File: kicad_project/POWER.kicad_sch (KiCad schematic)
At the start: 37 parts, among them Q1 S8050, Q2 BSS84, Q3 S8050, SW3 B3U-1000P, U2 SY8089A1AAC, U3 AXPM65611

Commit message: Pcb to production
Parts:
- removed D2: B5819W, Diode_SMD:D_SOD-123, symbol Device:D_Zener
- removed L7, L8: DFP252012TF-100M, smd-non-ipc:DFE252012P-1R0M=P2, symbol Device:L
- removed Q1, Q3: S8050, Package_TO_SOT_SMD:SOT-23, symbol Transistor_BJT:S8050
- removed Q2: BSS84, Package_TO_SOT_SMD:SOT-23, symbol Transistor_FET:IRF4905
- removed R30, R7: 100k, Resistor_SMD:R_0402_1005Metric, symbol Device:R
- removed R31: 680k, Resistor_SMD:R_0402_1005Metric, symbol Device:R
- removed SW3: B3U-1000P, hwlab:B3U-1000P, symbol Switch:SW_Push
- removed TP7: +5V, TestPoint:TestPoint_Pad_D1.0mm, symbol Connector:TestPoint
- removed U3: AXPM65611, smd-non-ipc:DFN-12, symbol Power_Display_oled:AXPM65611
- added C34, C36, C37: 22uF, Capacitor_SMD:C_0402_1005Metric, symbol Device:C
- added C35: 100nF, Capacitor_SMD:C_0402_1005Metric, symbol Device:C
- added D1: SS34, Diode_SMD:D_SMA, symbol Diode:SS34
- added DS3: GREEN, LED_SMD:LED_0603_1608Metric, symbol semi-opto-generic:LED-0603
- added L4: 1uH, smd-non-ipc:BR2518_YDN, symbol Device:L
- added L6: 22uH, smd-non-ipc:MDA7030-220M, symbol Device:L
- added R17: 22k, Resistor_SMD:R_0402_1005Metric, symbol Device:R
- added R18, R19: 0R, Resistor_SMD:R_0402_1005Metric, symbol Device:R
- added R20: 10k, Resistor_SMD:R_0402_1005Metric, symbol Device:R
- added R21: 80k6, Resistor_SMD:R_0402_1005Metric, symbol Device:R
- added R23: 1k, Resistor_SMD:R_0603_1608Metric_Pad0.98x0.95mm_HandSolder, symbol pasv-res:R-0603
- added U3: MT3608, Package_TO_SOT_SMD:SOT-23-6, symbol Regulator_Switching:MT3608
- added U4: SY8089A1AAC, smd-non-ipc:SOT95P285X130-5N, symbol SY8089A1AAC:SY8089A1AAC
- C18, C27, C30: value 10uF -> 22uF; BOM 10V 10uF X5R ±20% 0402 Multilayer Ceramic Capacitors MLCC -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 -> 10V 22uF X5R ±20% 0402 Multilayer Ceramic Capacitors MLCC -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; LCSC Part # C315248 -> C6119813; MPN CL05A106MP5NUNC -> CGA0402X5R226M100GT
- C28: value 1uF -> 22uF; footprint Capacitor_SMD:C_0603_1608Metric -> Capacitor_SMD:C_0402_1005Metric; BOM 16V 1uF X5R ±10% 0603 Multilayer Ceramic Capacitors MLCC - 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 -> 10V 22uF X5R ±20% 0402 Multilayer Ceramic Capacitors MLCC -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; LCSC Part # C1592 -> C6119813; MPN CL10A105KO8NNNC -> CGA0402X5R226M100GT
- C29: value 1uF -> 100nF; footprint Capacitor_SMD:C_0603_1608Metric -> Capacitor_SMD:C_0402_1005Metric; BOM 16V 1uF X5R ±10% 0603 Multilayer Ceramic Capacitors MLCC - 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 -> 35V 100nF X7R ±10% 0402 Multilayer Ceramic Capacitors MLCC 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; LCSC Part # C1592 -> C343047; MPN CL10A105KO8NNNC -> CGA2B3X7R1V104KT0Y0F
- C31: value 10uF -> 6.8pF; BOM 10V 10uF X5R ±20% 0402 Multilayer Ceramic Capacitors MLCC -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 -> 50V 6.8pF C0G 0402 Multilayer Ceramic Capacitors MLCC - SMD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; LCSC Part # C315248 -> C1576; MPN CL05A106MP5NUNC -> 0402CG6R8C500NT
- R10: value 22k -> 10k; BOM 62.5mW Thick Film Resistors 50V ±100ppm/℃ ±1% 22kΩ 0402 Chi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 -> 62.5mW Thick Film Resistors 50V ±100ppm/℃ ±5% 10kΩ 0402 Chi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; LCSC Part # C25768 -> C25531; MPN 0402WGF2202TCE -> 0402WGJ0103TCE
- R13, R14: value 0R -> 100k; BOM 62.5mW Thick Film Resistors 50V ±800ppm/℃ ±1% 0Ω 0402 Chip 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 -> 62.5mW Thick Film Resistors 50V ±100ppm/℃ ±1% 100kΩ 0402 Ch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; LCSC Part # C17168 -> C25741; MPN 0402WGF0000TCE -> 0402WGF1003TCE
- R9: value 100k -> 64k9; BOM 62.5mW Thick Film Resistors 50V ±100ppm/℃ ±1% 100kΩ 0402 Ch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 -> 63mW Thin Film Resistor 50V ±0.1% ±25ppm/℃ 64.9kΩ 0402 Chip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; LCSC Part # C25741 -> C490835; MPN 0402WGF1003TCE -> ERA2AEB6492X
- TP2: value +3V3 -> +4V6
- TP3: value +4V6 -> +5V4
- TP4: value -2V2 -> +3V3
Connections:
- net EAVDD is gone; now on net VBUS: C27.1
- net SWIRE is gone; now on net VCC: R13.2
- net +3V3: now also R18.2, R23.2; no longer C28.1, C29.1, R32.2, R7.2
- net 4.6V: now also R32.2, R7.2; no longer C31.1, TP3.1
- net GND: now also C34.2, C35.2, C36.2, C37.2, DS3.1 (K), R17.2, R20.2, U3.2 (GND), U4.2 (GND); no longer C31.2
- net VBUS: now also C28.1, C37.1, L6.1, U3.4 (EN), U3.5 (IN)
- net VCC: now also C29.1, C30.1, R19.2, U4.4 (IN); no longer R11.2
- net at R14.1: now also C31.1, TP4.1, C34.1, C35.1, C36.1, L4.2, R18.1
- net at R13.1: now also U4.1 (EN)
- net at C18.1: now also TP3.1, D1.1 (K), R19.1, R21.1
- removed net -2V2: C30.1, TP4.1
- net OL_EN: no longer names the net of R14.2
- net OL_EN: now also C31.2, R17.1, U4.5 (FB)
- new net: D1.2 (A), L6.2, U3.1 (SW)
- new net: R20.1, R21.2, U3.3 (FB)
- new net: L4.1, U4.3 (LX)
- new net: DS3.2 (A), R23.1
- new net DISPLAY_PWR_EN: R11.2
- no-connect marks 1 -> 0
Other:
- note added: "MAX INPUT: +5v5"
- note added: "POWER Supplies"
- note removed: "+4.6V"
- note removed: "-2.2V"
- note removed: "LATCH TURN ON CIRCUIT"
- note removed: "Power Supplies"
- moved on the sheet: C21, C22, C23, C24, C25, C26, DS1, L5, R11, R32, R7, R9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

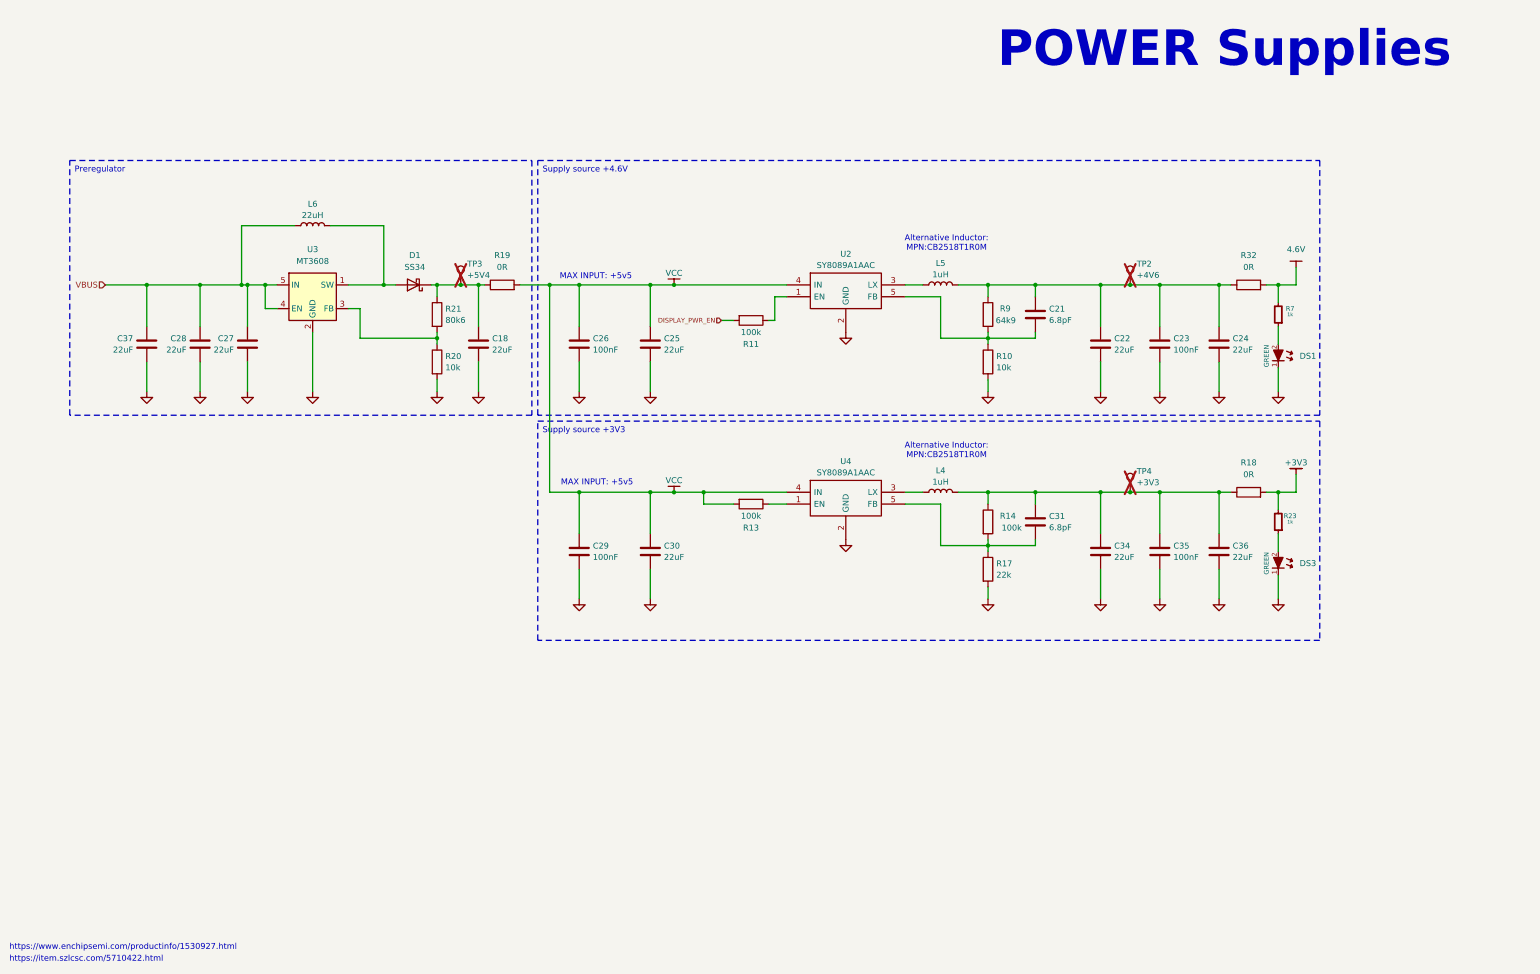
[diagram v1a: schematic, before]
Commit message: Remove USB preregulator from power circuit
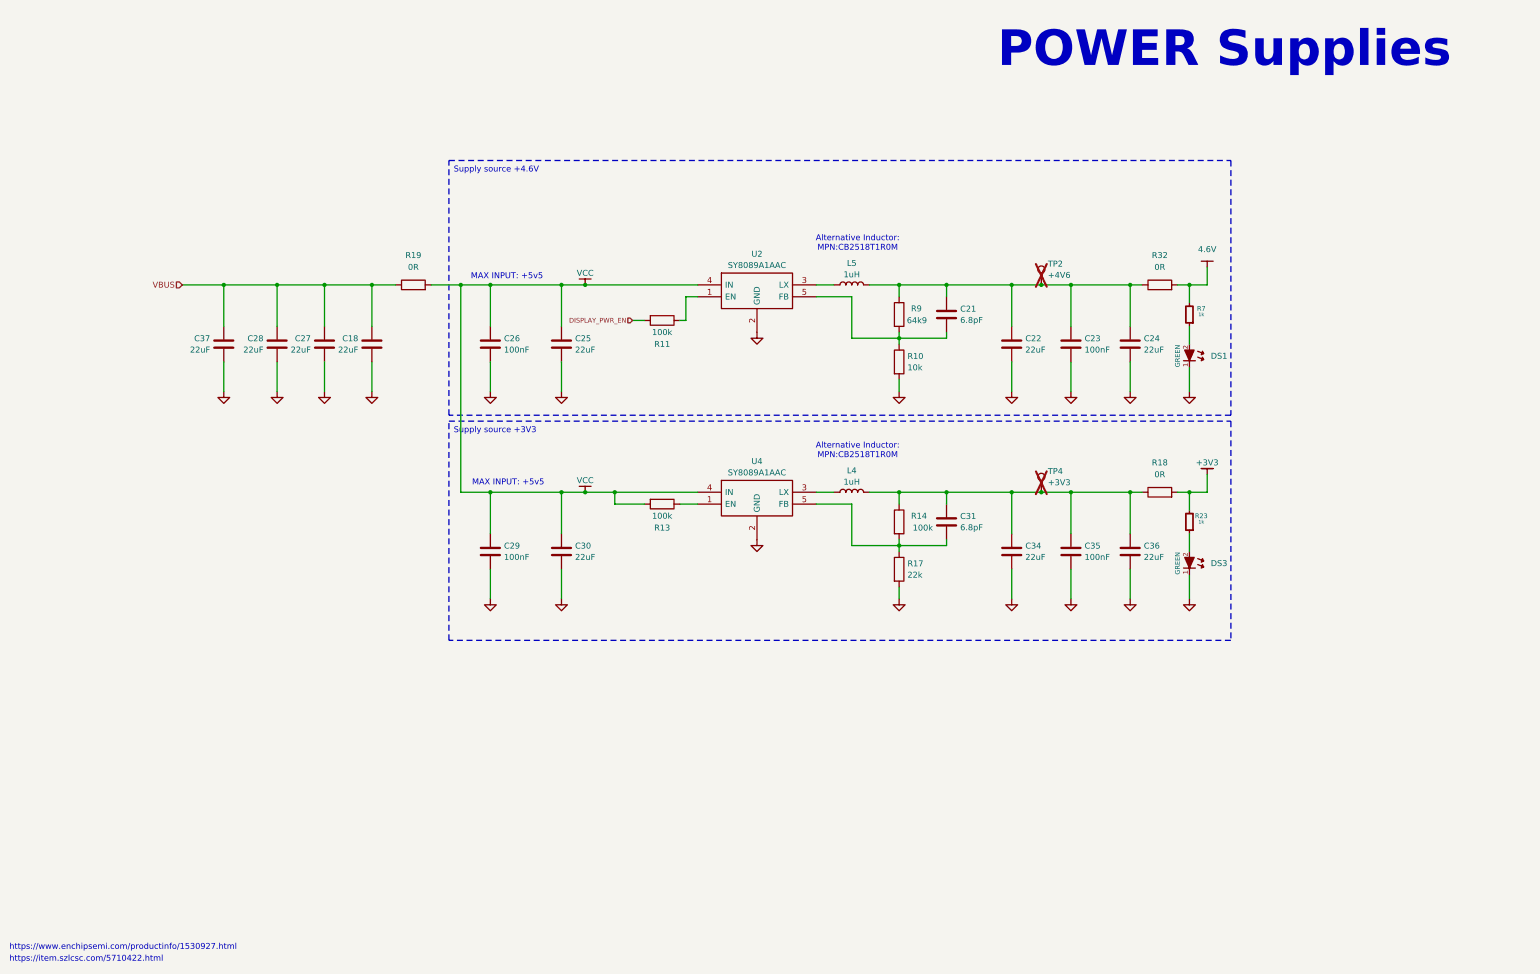
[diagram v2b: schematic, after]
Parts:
- removed D1: SS34, Diode_SMD:D_SMA, symbol Diode:SS34
- removed L6: 22uH, smd-non-ipc:MDA7030-220M, symbol Device:L
- removed R20: 10k, Resistor_SMD:R_0402_1005Metric, symbol Device:R
- removed R21: 80k6, Resistor_SMD:R_0402_1005Metric, symbol Device:R
- removed TP3: +5V4, TestPoint:TestPoint_Pad_D1.0mm, symbol Connector:TestPoint
- removed U3: MT3608, Package_TO_SOT_SMD:SOT-23-6, symbol Regulator_Switching:MT3608
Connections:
- net VBUS: now also C18.1, R19.1
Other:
- moved on the sheet: C18, C21, C22, C23, C24, C25, C26, C27, C28, C29, C30, C31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
